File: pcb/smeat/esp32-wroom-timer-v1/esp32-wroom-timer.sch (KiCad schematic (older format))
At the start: 56 parts, among them J1 Fan_connector, J2 Conn_01x06_Male, J3 input power, Q1 Q_NMOS_GSD, Q2 Q_NMOS_GSD, U1 ESP32-WROOM-32, U2 AMS1117, U3 RX5808, U4 MP1584, U5 RX5808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

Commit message: Update.
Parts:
- added C23, C24: 10µF, Capacitor_SMD:C_0805_2012Metric, symbol Device:C
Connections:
- wire segments 186 -> 190
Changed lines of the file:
@@
 Text Notes 7850 5200 0    20   ~ 0
 Not sure if this pin is able to take >6V. \nThe datasheet isn't clear about this
+$Comp
+L power:+3.3V #PWR022
+U 1 1 5D4229A1
+P 4100 1200
+F 0 "#PWR022" H 4100 1050 50  0001 C CNN
+F 1 "+3.3V" H 4115 1373 50  0000 C CNN
+F 2 "" H 4100 1200 50  0001 C CNN
+F 3 "" H 4100 1200 50  0001 C CNN
+	1    4100 1200
+	1    0    0    -1
+$EndComp
+$Comp
+L Device:C C23
+U 1 1 5D422E98
+P 3800 1500
+F 0 "C23" V 3650 1500 50  0000 C CNN
+F 1 "10µF" V 3950 1600 50  0000 C CNN
+F 2 "Capacitor_SMD:C_0805_2012Metric" H 3838 1350 50  0001 C CNN
+F 3 "~" H 3800 1500 50  0001 C CNN
+	1    3800 1500
+	-1   0    0    1
+$EndComp
+$Comp
+L Device:C C24
+U 1 1 5D423338
+P 4100 1500
+F 0 "C24" V 3950 1500 50  0000 C CNN
+F 1 "10µF" V 4250 1600 50  0000 C CNN
+F 2 "Capacitor_SMD:C_0805_2012Metric" H 4138 1350 50  0001 C CNN
+F 3 "~" H 4100 1500 50  0001 C CNN
+	1    4100 1500
+	-1   0    0    1
+$EndComp
+$Comp
+L power:GND #PWR023
+U 1 1 5D4239EF
+P 4100 1850
+F 0 "#PWR023" H 4100 1600 50  0001 C CNN
+F 1 "GND" H 4105 1677 50  0000 C CNN
+F 2 "" H 4100 1850 50  0001 C CNN
+F 3 "" H 4100 1850 50  0001 C CNN
+	1    4100 1850
+	1    0    0    -1
+$EndComp
+Wire Wire Line
+	3800 1650 4100 1650
+Connection ~ 4100 1650
+Wire Wire Line
+	4100 1350 3800 1350
+Connection ~ 4100 1350
+Wire Wire Line
+	4100 1200 4100 1350
+Wire Wire Line
+	4100 1650 4100 1850
 $EndSCHEMATC

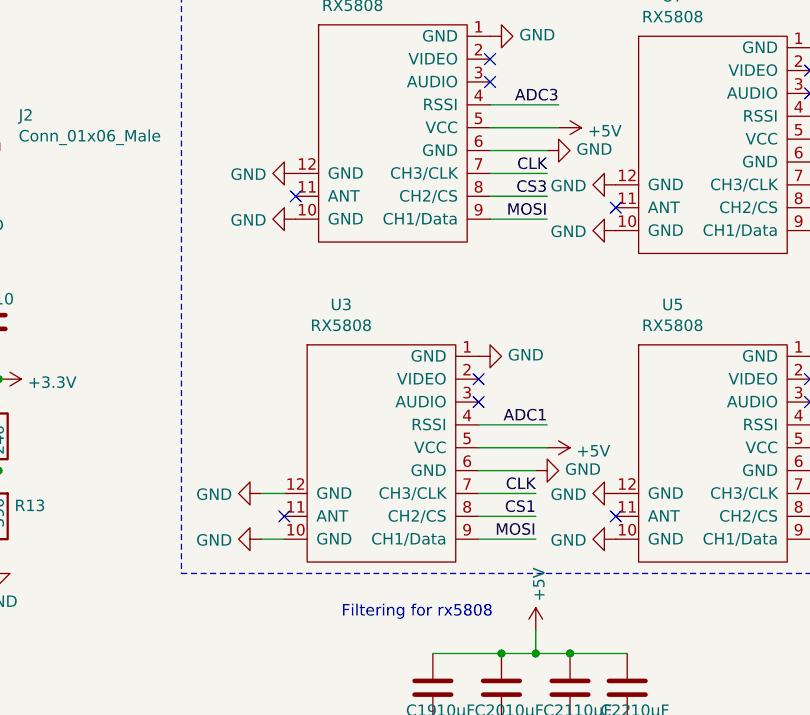
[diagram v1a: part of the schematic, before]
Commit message: Disconnect antenna ground from the global ground plane.
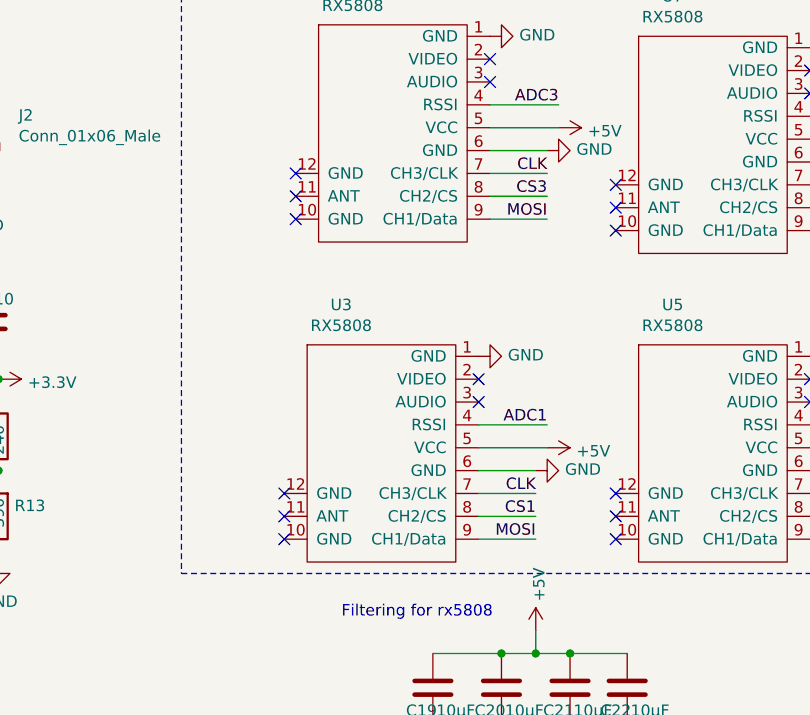
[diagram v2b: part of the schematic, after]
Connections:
- wire segments 190 -> 188
- no-connect marks 27 -> 35
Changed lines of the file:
@@
 	0    -1   -1   0
 $EndComp
-$Comp
-L power:GND #PWR0112
-U 1 1 5D3B2156
-P 8150 2950
-F 0 "#PWR0112" H 8150 2700 50  0001 C CNN
-F 1 "GND" V 8155 2822 50  0000 R CNN
-F 2 "" H 8150 2950 50  0001 C CNN
-F 3 "" H 8150 2950 50  0001 C CNN
-	1    8150 2950
-	0    1    1    0
-$EndComp
-$Comp
-L my_components:RX5808 U3
-U 1 1 5D3A2DAA
-P 8700 2200
-F 0 "U3" H 8499 2475 50  0000 C CNN
-F 1 "RX5808" H 8499 2384 50  0000 C CNN
-F 2 "my:rx5808" H 8700 2150 50  0001 C CNN
-F 3 "" H 8700 2150 50  0001 C CNN
-	1    8700 2200
-	1    0    0    -1
-$EndComp
-Wire Wire Line
-	8150 2950 8250 2950
-$Comp
-L power:GND #PWR0113
-U 1 1 5D3B81DB
-P 8150 2750
-F 0 "#PWR0113" H 8150 2500 50  0001 C CNN
-F 1 "GND" V 8155 2622 50  0000 R CNN
-F 2 "" H 8150 2750 50  0001 C CNN
-F 3 "" H 8150 2750 50  0001 C CNN
-	1    8150 2750
-	0    1    1    0
-$EndComp
-Wire Wire Line
-	8150 2750 8250 2750
 Wire Wire Line
 	1800 7350 1800 7250
@@
 $EndComp
 $Comp
-L power:GND #PWR0133
-U 1 1 5D3C4A63
-P 8300 1350
-F 0 "#PWR0133" H 8300 1100 50  0001 C CNN
-F 1 "GND" V 8305 1222 50  0000 R CNN
-F 2 "" H 8300 1350 50  0001 C CNN
-F 3 "" H 8300 1350 50  0001 C CNN
-	1    8300 1350
-	0    1    1    0
-$EndComp
-$Comp
-L power:GND #PWR0134
-U 1 1 5D3C511D
-P 8300 1550
-F 0 "#PWR0134" H 8300 1300 50  0001 C CNN
-F 1 "GND" V 8305 1422 50  0000 R CNN
-F 2 "" H 8300 1550 50  0001 C CNN
-F 3 "" H 8300 1550 50  0001 C CNN
-	1    8300 1550
-	0    1    1    0
-$EndComp
-$Comp
 L power:GND #PWR0135
 U 1 1 5D3C5498
@@
 	1    10550 2150
 	0    -1   -1   0
-$EndComp
-$Comp
-L power:GND #PWR0136
-U 1 1 5D3C618C
-P 9700 2750
-F 0 "#PWR0136" H 9700 2500 50  0001 C CNN
-F 1 "GND" V 9705 2622 50  0000 R CNN
-F 2 "" H 9700 2750 50  0001 C CNN
-F 3 "" H 9700 2750 50  0001 C CNN
-	1    9700 2750
-	0    1    1    0
-$EndComp
-$Comp
-L power:GND #PWR0137
-U 1 1 5D3C6EAE
-P 9700 2950
-F 0 "#PWR0137" H 9700 2700 50  0001 C CNN
-F 1 "GND" V 9705 2822 50  0000 R CNN
-F 2 "" H 9700 2950 50  0001 C CNN
-F 3 "" H 9700 2950 50  0001 C CNN
-	1    9700 2950
-	0    1    1    0
-$EndComp
-$Comp
-L power:GND #PWR0138
-U 1 1 5D3C7409
-P 9700 1600
-F 0 "#PWR0138" H 9700 1350 50  0001 C CNN
-F 1 "GND" V 9705 1472 50  0000 R CNN
-F 2 "" H 9700 1600 50  0001 C CNN
-F 3 "" H 9700 1600 50  0001 C CNN
-	1    9700 1600
-	0    1    1    0
-$EndComp
-$Comp
-L power:GND #PWR0139
-U 1 1 5D3C7937
-P 9700 1400
-F 0 "#PWR0139" H 9700 1150 50  0001 C CNN
-F 1 "GND" V 9705 1272 50  0000 R CNN
-F 2 "" H 9700 1400 50  0001 C CNN
-F 3 "" H 9700 1400 50  0001 C CNN
-	1    9700 1400
-	0    1    1    0
 $EndComp
 $Comp
@@
 Wire Wire Line
 	4100 1650 4100 1850
+$Comp
+L my_components:RX5808 U3
+U 1 1 5D3A2DAA
+P 8700 2200
+F 0 "U3" H 8499 2475 50  0000 C CNN
+F 1 "RX5808" H 8499 2384 50  0000 C CNN
+F 2 "my:rx5808" H 8700 2150 50  0001 C CNN
+F 3 "" H 8700 2150 50  0001 C CNN
+	1    8700 2200
+	1    0    0    -1
+$EndComp
+NoConn ~ 8250 2950
+NoConn ~ 8250 2750
+NoConn ~ 8300 1350
+NoConn ~ 8300 1550
+NoConn ~ 9700 1400
+NoConn ~ 9700 1600
+NoConn ~ 9700 2750
+NoConn ~ 9700 2950
 $EndSCHEMATC
